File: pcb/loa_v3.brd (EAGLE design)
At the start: 50.9 x 81.4 mm, 111 parts, among them IC1 STM32F10XVXT6, IC2 M25P80MW, IC3 NAND_FLASH, IC4 MCP1825S-1202E/DB, IC5 NCP3170, IC6 AD7266SU, Q2 50.000, Q3 25.000, U1 6SLX9TQG144, X3 MINI-USB

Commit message: Cleanup
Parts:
- JP8: value (none) -> GND
- SJ2: value (none) -> WP
- SJ3: value (none) -> AGND-GND
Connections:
- net N$37 renamed VDDA
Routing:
- net P94: track 20.2 -> 22.2 mm
- net +3V3: track 630.6 -> 631.6 mm, vias 39 -> 40
- net GND: track 244.8 -> 245.7 mm, vias 55 -> 56
- net P93: track 17.7 -> 18.4 mm
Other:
- board text added: "GND"
- board text removed: "optional"
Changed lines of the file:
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@@
 <setting verticaltext="up"/>
 </settings>
-<grid distance="0.635" unitdist="mm" unit="mm" style="dots" multiple="1" display="yes" altdistance="0.00625" altunitdist="inch" altunit="inch"/>
+<grid distance="0.635" unitdist="mm" unit="mm" style="dots" multiple="1" display="yes" altdistance="0.003125" altunitdist="inch" altunit="inch"/>
 <layers>
 <layer number="1" name="Top" color="4" fill="1" visible="yes" active="yes"/>
@@
 <wire x1="38.5763" y1="2.3813" x2="37.9413" y2="3.0163" width="0.254" layer="49"/>
 <wire x1="37.9413" y1="3.0163" x2="37.3063" y2="2.3813" width="0.254" layer="49"/>
-<circle x="41.5926" y="6.9851" radius="0.3549" width="0.3048" layer="1"/>
+<circle x="42.2276" y="6.6676" radius="0.3549" width="0.3048" layer="1"/>
 <circle x="40.4813" y="80.4069" radius="0.2245" width="0.3048" layer="1"/>
 <circle x="41.5131" y="80.0894" radius="0.2245" width="0.3048" layer="1"/>
@@
 <text x="13.97" y="19.2882" size="0.8128" layer="1" ratio="20" rot="SR270">05/2014</text>
 <text x="42.97995" y="77.62325" size="1.016" layer="1" ratio="15">v3</text>
-<text x="29.05125" y="78.26375" size="1.016" layer="21" ratio="12">optional</text>
 <circle x="18.57385" y="73.81885" radius="0.3549" width="0.3048" layer="1"/>
+<text x="12.54125" y="78.4225" size="1.016" layer="1" font="vector" ratio="15" rot="SR90">GND</text>
 </plain>
 <attributes>
@@
 <element name="C1" library="rcl" package="C0603" value="100n" x="39.37" y="77.47" rot="MR0"/>
 <element name="C2" library="rcl" package="C0603" value="100n" x="39.37" y="53.975" rot="MR0"/>
-<element name="SJ2" library="rca_sontiges" package="SJ_2S" value="" x="38.25875" y="49.53" rot="MR0"/>
-<element name="SJ3" library="rca_sontiges" package="SJS" value="" x="12.065" y="69.5325" rot="MR180"/>
+<element name="SJ2" library="rca_sontiges" package="SJ_2S" value="WP" x="38.25875" y="49.53" rot="MR0"/>
+<element name="SJ3" library="rca_sontiges" package="SJS" value="AGND-GND" x="12.065" y="69.5325" rot="MR180"/>
 <element name="JP7" library="pinhead2" package="2X16" value="" x="48.26" y="20.32" rot="R270"/>
-<element name="JP8" library="pinhead2" package="1X01" value="" x="13.97" y="80.01"/>
+<element name="JP8" library="pinhead2" package="1X01" value="GND" x="13.97" y="80.01"/>
 </elements>
 <signals>
@@
 <wire x1="10.0013" y1="39.5288" x2="10.0013" y2="39.8462" width="0.8128" layer="16"/>
 <wire x1="10.0013" y1="39.8462" x2="10.00125" y2="40.3225" width="0.8128" layer="16"/>
-<wire x1="39.6" y1="23.5825" x2="37.845" y2="23.5825" width="0.3048" layer="1"/>
-<wire x1="40.005" y1="23.1775" x2="39.6" y2="23.5825" width="0.3048" layer="1"/>
-<wire x1="40.5374" y1="23.1775" x2="40.005" y2="23.1775" width="0.3048" layer="1"/>
+<wire x1="39.75875" y1="23.5825" x2="37.845" y2="23.5825" width="0.3048" layer="1"/>
+<wire x1="40.16375" y1="23.1775" x2="39.75875" y2="23.5825" width="0.3048" layer="1"/>
+<wire x1="40.5374" y1="23.1775" x2="40.16375" y2="23.1775" width="0.3048" layer="1"/>
 <wire x1="40.6399" y1="23.28" x2="40.5374" y2="23.1775" width="0.3048" layer="1"/>
 <wire x1="40.6399" y1="23.0189" x2="40.6399" y2="23.28" width="0.3048" layer="1"/>
@@
 <wire x1="13.81125" y1="69.5325" x2="13.97" y2="69.69125" width="0.3048" layer="16"/>
 <contactref element="JP8" pad="1"/>
+<via x="41.671875" y="23.33625" extent="1-16" drill="0.3048"/>
+<wire x1="41.671875" y1="23.33625" x2="40.69635" y2="23.33625" width="0.6096" layer="1"/>
 </signal>
 <signal name="+3V3">
@@
 <wire x1="30.4801" y1="29.185" x2="30.8437" y2="29.2813" width="0.8128" layer="16"/>
 <wire x1="27.4637" y1="30.06" x2="27.5038" y2="30.1001" width="0.8128" layer="16"/>
-<wire x1="37.845" y1="24.0825" x2="39.4812" y2="24.0825" width="0.3048" layer="1"/>
-<wire x1="39.4812" y1="24.0825" x2="40.3225" y2="24.9238" width="0.3048" layer="1"/>
-<wire x1="40.3225" y1="24.9238" x2="40.5837" y2="24.9238" width="0.3048" layer="1"/>
+<wire x1="37.845" y1="24.0825" x2="39.63995" y2="24.0825" width="0.3048" layer="1"/>
+<wire x1="39.63995" y1="24.0825" x2="40.48125" y2="24.9238" width="0.3048" layer="1"/>
+<wire x1="40.48125" y1="24.9238" x2="40.5837" y2="24.9238" width="0.3048" layer="1"/>
 <wire x1="40.5837" y1="24.9238" x2="40.6399" y2="24.98" width="0.3048" layer="1"/>
 <wire x1="37.845" y1="21.5825" x2="39.4651" y2="21.5825" width="0.3048" layer="1"/>
@@
 <wire x1="40.6399" y1="24.98" x2="40.6399" y2="24.92385" width="0.6096" layer="1"/>
 <wire x1="40.6399" y1="24.92385" x2="40.79875" y2="24.765" width="0.6096" layer="1"/>
-<wire x1="40.79875" y1="24.765" x2="41.75125" y2="24.765" width="0.6096" layer="1"/>
-<via x="41.75125" y="24.765" extent="1-16" drill="0.3048"/>
+<wire x1="40.79875" y1="24.765" x2="41.671875" y2="24.765" width="0.6096" layer="1"/>
+<via x="41.671875" y="24.765" extent="1-16" drill="0.3048"/>
 <via x="10.0012" y="21.2725" extent="1-16" drill="0.5"/>
 <wire x1="9.0487" y1="20.32" x2="9.04875" y2="20.32" width="0.8128" layer="1"/>
@@
 <vertex x="11.58875" y="26.19375"/>
 </polygon>
+<via x="39.449375" y="22.939375" extent="1-16" drill="0.3048"/>
+<wire x1="39.84625" y1="21.9075" x2="39.449375" y2="22.939375" width="0.6096" layer="1"/>
 </signal>
 <signal name="!RESET">
@@
 <via x="35.4012" y="19.2088" extent="1-16" drill="0.3048"/>
 </signal>
-<signal name="N$37">
+<signal name="VDDA">
 <contactref element="IC1" pad="22"/>
 <contactref element="C63" pad="1"/>
@@
 <wire x1="34.76625" y1="67.46875" x2="36.67125" y2="69.37375" width="0.254" layer="1"/>
 <contactref element="JP6" pad="12"/>
-<wire x1="36.67125" y1="69.37375" x2="43.02125" y2="69.37375" width="0.254" layer="1"/>
-<wire x1="43.02125" y1="69.37375" x2="46.355" y2="66.04" width="0.254" layer="1"/>
-<wire x1="46.355" y1="66.04" x2="48.26" y2="66.04" width="0.254" layer="1"/>
+<wire x1="36.67125" y1="69.37375" x2="39.21125" y2="69.37375" width="0.254" layer="1"/>
+<wire x1="39.21125" y1="69.37375" x2="42.545" y2="66.04" width="0.254" layer="1"/>
+<wire x1="42.545" y1="66.04" x2="48.26" y2="66.04" width="0.254" layer="1"/>
 <wire x1="48.26" y1="66.04" x2="49.53" y2="67.31" width="0.254" layer="1"/>
 </signal>
@@
 <wire x1="34.29" y1="67.78625" x2="36.35375" y2="69.85" width="0.254" layer="1"/>
 <contactref element="JP6" pad="11"/>
-<wire x1="36.35375" y1="69.85" x2="44.45" y2="69.85" width="0.254" layer="1"/>
-<wire x1="44.45" y1="69.85" x2="46.99" y2="67.31" width="0.254" layer="1"/>
+<wire x1="36.35375" y1="69.85" x2="39.37" y2="69.85" width="0.254" layer="1"/>
+<wire x1="39.37" y1="69.85" x2="42.70375" y2="66.51625" width="0.254" layer="1"/>
+<wire x1="42.70375" y1="66.51625" x2="46.19625" y2="66.51625" width="0.254" layer="1"/>
+<wire x1="46.19625" y1="66.51625" x2="46.99" y2="67.31" width="0.254" layer="1"/>
 </signal>
 <signal name="P94">
 <contactref element="U1" pad="P94"/>
 <contactref element="JP6" pad="10"/>
-<wire x1="36.228375" y1="70.3263" x2="43.815" y2="70.3263" width="0.254" layer="1"/>
-<wire x1="43.815" y1="70.3263" x2="45.72" y2="70.32625" width="0.254" layer="1"/>
-<wire x1="45.72" y1="70.32625" x2="46.275625" y2="70.881875" width="0.254" layer="1"/>
-<wire x1="46.275625" y1="70.881875" x2="48.498125" y2="70.881875" width="0.254" layer="1"/>
-<wire x1="48.498125" y1="70.881875" x2="49.53" y2="69.85" width="0.254" layer="1"/>
+<wire x1="36.228375" y1="70.3263" x2="39.5287" y2="70.3263" width="0.254" layer="1"/>
+<wire x1="48.180625" y1="68.500625" x2="49.53" y2="69.85" width="0.254" layer="1"/>
 <wire x1="32.127046875" y1="65.748721875" x2="33.81375" y2="67.435425" width="0.254" layer="1"/>
 <wire x1="33.81375" y1="67.435425" x2="33.81375" y2="67.945" width="0.254" layer="1"/>
 <wire x1="33.81375" y1="67.945" x2="36.228375" y2="70.3263" width="0.254" layer="1"/>
+<wire x1="48.180625" y1="68.500625" x2="46.593125" y2="68.500625" width="0.254" layer="1"/>
+<wire x1="46.593125" y1="68.500625" x2="45.085" y2="66.9925" width="0.254" layer="1"/>
+<wire x1="45.085" y1="66.9925" x2="42.8625" y2="66.9925" width="0.254" layer="1"/>
+<wire x1="42.8625" y1="66.9925" x2="39.5287" y2="70.3263" width="0.254" layer="1"/>
 </signal>
 <signal name="P95">

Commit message: Changed logo to reflect the version number
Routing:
- net +3V3: track 631.6 -> 635.4 mm
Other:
- board text added: "v3.0"
- board text removed: "v3"
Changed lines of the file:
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@@
 <?xml version="1.0" encoding="utf-8"?>
 <!DOCTYPE eagle SYSTEM "eagle.dtd">
-<eagle version="6.5.0">
+<eagle version="6.4">
 <drawing>
 <settings>
@@
 <setting verticaltext="up"/>
 </settings>
-<grid distance="0.635" unitdist="mm" unit="mm" style="dots" multiple="1" display="yes" altdistance="0.003125" altunitdist="inch" altunit="inch"/>
+<grid distance="0.635" unitdist="mm" unit="mm" style="dots" multiple="1" display="yes" altdistance="0.00625" altunitdist="inch" altunit="inch"/>
 <layers>
 <layer number="1" name="Top" color="4" fill="1" visible="yes" active="yes"/>
@@
 <wire x1="37.9413" y1="3.0163" x2="37.3063" y2="2.3813" width="0.254" layer="49"/>
 <circle x="42.2276" y="6.6676" radius="0.3549" width="0.3048" layer="1"/>
-<circle x="40.4813" y="80.4069" radius="0.2245" width="0.3048" layer="1"/>
-<circle x="41.5131" y="80.0894" radius="0.2245" width="0.3048" layer="1"/>
+<circle x="40.401925" y="80.0894" radius="0.2245" width="0.3048" layer="1"/>
+<circle x="41.1956" y="80.645025" radius="0.2245" width="0.3048" layer="1"/>
 <circle x="38.5762" y="79.4544" radius="0.3" width="0.254" layer="1"/>
 <text x="19.2088" y="0.635" size="1.27" layer="1" ratio="15">R</text>
 <text x="39.68745" y="34.29015" size="1.4224" layer="1" ratio="15" rot="R180">fg</text>
 <text x="13.97" y="19.2882" size="0.8128" layer="1" ratio="20" rot="SR270">05/2014</text>
-<text x="42.97995" y="77.62325" size="1.016" layer="1" ratio="15">v3</text>
+<text x="38.21745" y="74.607" size="1.016" layer="1" ratio="15">v3.0</text>
 <circle x="18.57385" y="73.81885" radius="0.3549" width="0.3048" layer="1"/>
 <text x="12.54125" y="78.4225" size="1.016" layer="1" font="vector" ratio="15" rot="SR90">GND</text>
+<circle x="41.8306" y="79.851275" radius="0.2245" width="0.3048" layer="1"/>
 </plain>
 <attributes>
@@
 <wire x1="45.9581" y1="75.9618" x2="45.72" y2="76.3588" width="0.3048" layer="1" curve="36.872784"/>
 <wire x1="45.72" y1="76.3588" x2="42.7038" y2="77.1525" width="0.3048" layer="1"/>
-<wire x1="42.7038" y1="77.1525" x2="41.4338" y2="77.9463" width="0.3048" layer="1"/>
-<wire x1="42.5451" y1="78.7401" x2="41.4338" y2="77.9463" width="0.3048" layer="1"/>
-<wire x1="42.5451" y1="79.0576" x2="42.5451" y2="78.7401" width="0.3048" layer="1"/>
-<wire x1="42.3863" y1="79.2163" x2="42.5451" y2="79.0576" width="0.3048" layer="1"/>
-<wire x1="42.0688" y1="79.2163" x2="42.3863" y2="79.2163" width="0.3048" layer="1"/>
-<wire x1="40.7988" y1="78.5813" x2="41.1163" y2="78.74" width="0.3048" layer="1"/>
-<wire x1="41.1163" y1="78.74" x2="42.0688" y2="79.2163" width="0.3048" layer="1"/>
-<wire x1="39.8463" y1="78.5813" x2="40.4813" y2="78.5813" width="0.3048" layer="1"/>
-<wire x1="40.4813" y1="78.5813" x2="40.7988" y2="78.5813" width="0.3048" layer="1"/>
+<wire x1="42.7038" y1="77.1525" x2="41.671925" y2="77.78755" width="0.3048" layer="1"/>
+<wire x1="42.70385" y1="78.58135" x2="41.671925" y2="77.78755" width="0.3048" layer="1"/>
+<wire x1="42.70385" y1="78.89885" x2="42.70385" y2="78.58135" width="0.3048" layer="1"/>
+<wire x1="42.465675" y1="79.05755" x2="42.70385" y2="78.89885" width="0.3048" layer="1"/>
+<wire x1="42.148175" y1="79.05755" x2="42.465675" y2="79.05755" width="0.3048" layer="1"/>
+<wire x1="40.7988" y1="78.5813" x2="40.91783125" y2="78.620953125" width="0.3048" layer="1"/>
+<wire x1="40.91783125" y1="78.620953125" x2="41.036925" y2="78.660625" width="0.3048" layer="1"/>
+<wire x1="41.036925" y1="78.660625" x2="41.65031875" y2="78.879721875" width="0.3048" layer="1"/>
+<wire x1="41.65031875" y1="78.879721875" x2="42.148175" y2="79.05755" width="0.3048" layer="1"/>
+<wire x1="39.8463" y1="78.5813" x2="40.7988" y2="78.5813" width="0.3048" layer="1"/>
 <wire x1="39.8463" y1="79.2163" x2="39.8463" y2="78.5813" width="0.3048" layer="1"/>
 <wire x1="39.5289" y1="80.1688" x2="39.8463" y2="79.2163" width="0.3048" layer="1" curve="-30.476126"/>
@@
 <wire x1="39.8463" y1="77.6288" x2="39.5288" y2="77.9463" width="0.3048" layer="1"/>
 <wire x1="38.5763" y1="76.6763" x2="39.8463" y2="77.6288" width="0.3048" layer="1"/>
-<wire x1="40.4813" y1="78.5813" x2="40.4813" y2="80.1688" width="0.254" layer="1"/>
-<wire x1="41.1163" y1="78.74" x2="41.4338" y2="79.8513" width="0.254" layer="1"/>
-<wire x1="41.1163" y1="78.74" x2="40.7988" y2="77.6288" width="0.254" layer="1"/>
-<wire x1="40.4813" y1="78.5813" x2="40.4813" y2="77.9463" width="0.254" layer="1"/>
 <wire x1="40.22" y1="77.47" x2="40.0612" y2="77.6288" width="0.3048" layer="16"/>
 <wire x1="40.0612" y1="77.6288" x2="39.8463" y2="77.6288" width="0.3048" layer="16"/>
@@
 <via x="39.449375" y="22.939375" extent="1-16" drill="0.3048"/>
 <wire x1="39.84625" y1="21.9075" x2="39.449375" y2="22.939375" width="0.6096" layer="1"/>
+<wire x1="41.195625" y1="77.866875" x2="41.75125" y2="79.6925" width="0.254" layer="1"/>
+<wire x1="41.11625" y1="80.406875" x2="40.878125" y2="78.184375" width="0.254" layer="1"/>
+<wire x1="40.401875" y1="79.85125" x2="40.48125" y2="77.94625" width="0.254" layer="1"/>
+<wire x1="40.878125" y1="78.184375" x2="40.91783125" y2="78.620953125" width="0.254" layer="1"/>
+<wire x1="41.195625" y1="77.866875" x2="41.513125" y2="78.819375" width="0.254" layer="1"/>
+<wire x1="41.513125" y1="78.819375" x2="41.65031875" y2="78.879721875" width="0.254" layer="1"/>
+<wire x1="40.48125" y1="77.94625" x2="40.48125" y2="78.58125" width="0.254" layer="1"/>
+<wire x1="40.48125" y1="78.58125" x2="40.16375" y2="78.58125" width="0.254" layer="1"/>
 </signal>
 <signal name="!RESET">
@@
 <wire x1="16.9864" y1="29.6863" x2="16.9864" y2="30.0038" width="0.254" layer="16"/>
 <wire x1="16.9864" y1="30.0038" x2="27.305" y2="40.3225" width="0.254" layer="16"/>
-<wire x1="27.305" y1="40.3225" x2="31.115" y2="40.3225" width="0.254" layer="16"/>
-<wire x1="31.115" y1="40.3225" x2="33.65505" y2="42.86255" width="0.254" layer="16"/>
+<wire x1="27.305" y1="40.3225" x2="27.46375" y2="40.48125" width="0.254" layer="16"/>
+<wire x1="27.46375" y1="40.48125" x2="31.27375" y2="40.48125" width="0.254" layer="16"/>
+<wire x1="31.27375" y1="40.48125" x2="33.65505" y2="42.86255" width="0.254" layer="16"/>
 <wire x1="18.09745" y1="29.6863" x2="16.9864" y2="29.6863" width="0.254" layer="1"/>
 <wire x1="18.70125" y1="29.0825" x2="18.09745" y2="29.6863" width="0.254" layer="1"/>
@@
 <wire x1="17.62125" y1="29.21" x2="17.6213" y2="29.3688" width="0.254" layer="16"/>
 <wire x1="17.6213" y1="29.3688" x2="17.6213" y2="30.0038" width="0.254" layer="16"/>
-<wire x1="17.6213" y1="30.0038" x2="25.55875" y2="37.94125" width="0.254" layer="16"/>
+<wire x1="17.6213" y1="30.0038" x2="25.4" y2="37.7825" width="0.254" layer="16"/>
 <via x="17.2245" y="28.8131" extent="1-16" drill="0.3048"/>
 <contactref element="RN4" pad="1"/>
-<wire x1="25.55875" y1="37.94125" x2="27.94" y2="37.94125" width="0.254" layer="16"/>
+<wire x1="25.4" y1="37.7825" x2="27.78125" y2="37.7825" width="0.254" layer="16"/>
 <wire x1="28.8237" y1="39.3583" x2="28.8237" y2="38.82495" width="0.254" layer="1"/>
 <wire x1="28.8237" y1="38.82495" x2="28.41625" y2="38.4175" width="0.254" layer="1"/>
 <via x="28.41625" y="38.4175" extent="1-16" drill="0.3048"/>
 <wire x1="28.41625" y1="38.4175" x2="28.09875" y2="38.1" width="0.254" layer="16"/>
-<wire x1="27.94" y1="37.94125" x2="28.41625" y2="38.4175" width="0.254" layer="16"/>
+<wire x1="27.78125" y1="37.7825" x2="28.41625" y2="38.4175" width="0.254" layer="16"/>
 </signal>
 <signal name="FSMC_D15">
@@
 <wire x1="26.51125" y1="40.16375" x2="26.5112" y2="41.2749" width="0.254" layer="1"/>
 <wire x1="26.5112" y1="41.2749" x2="26.5113" y2="41.275" width="0.254" layer="1"/>
-<wire x1="26.5113" y1="41.275" x2="30.7975" y2="41.275" width="0.254" layer="16"/>
-<wire x1="30.7975" y1="41.275" x2="33.33755" y2="43.81505" width="0.254" layer="16"/>
+<wire x1="26.5113" y1="41.275" x2="26.67" y2="41.43375" width="0.254" layer="16"/>
+<wire x1="26.67" y1="41.43375" x2="30.95625" y2="41.43375" width="0.254" layer="16"/>
+<wire x1="30.95625" y1="41.43375" x2="33.33755" y2="43.81505" width="0.254" layer="16"/>
 <via x="26.5113" y="41.275" extent="1-16" drill="0.3048"/>
 <contactref element="RN6" pad="2"/>
@@
 <wire x1="24.92375" y1="39.68755" x2="26.03505" y2="39.68755" width="0.254" layer="16"/>
 <wire x1="26.03505" y1="39.68755" x2="27.14625" y2="40.79875" width="0.254" layer="16"/>
-<wire x1="27.14625" y1="40.79875" x2="30.95625" y2="40.79875" width="0.254" layer="16"/>
-<wire x1="30.95625" y1="40.79875" x2="33.49625" y2="43.33875" width="0.254" layer="16"/>
+<wire x1="27.14625" y1="40.79875" x2="27.305" y2="40.9575" width="0.254" layer="16"/>
+<wire x1="27.305" y1="40.9575" x2="31.115" y2="40.9575" width="0.254" layer="16"/>
+<wire x1="31.115" y1="40.9575" x2="33.49625" y2="43.33875" width="0.254" layer="16"/>
 <wire x1="33.49625" y1="43.33875" x2="37.30625" y2="43.33875" width="0.254" layer="16"/>
 <via x="24.92375" y="39.68755" extent="1-16" drill="0.3048"/>

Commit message: Added BOM attributes
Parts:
- C57, C58: value 470n -> 1µ
- IC3: value NAND_FLASH -> S34ML04G100TFI000
- IC6: value AD7266SU -> AD7265SU
- L2, L4: value 0,68u -> 0,47u
- LED2: value Red -> Yellow

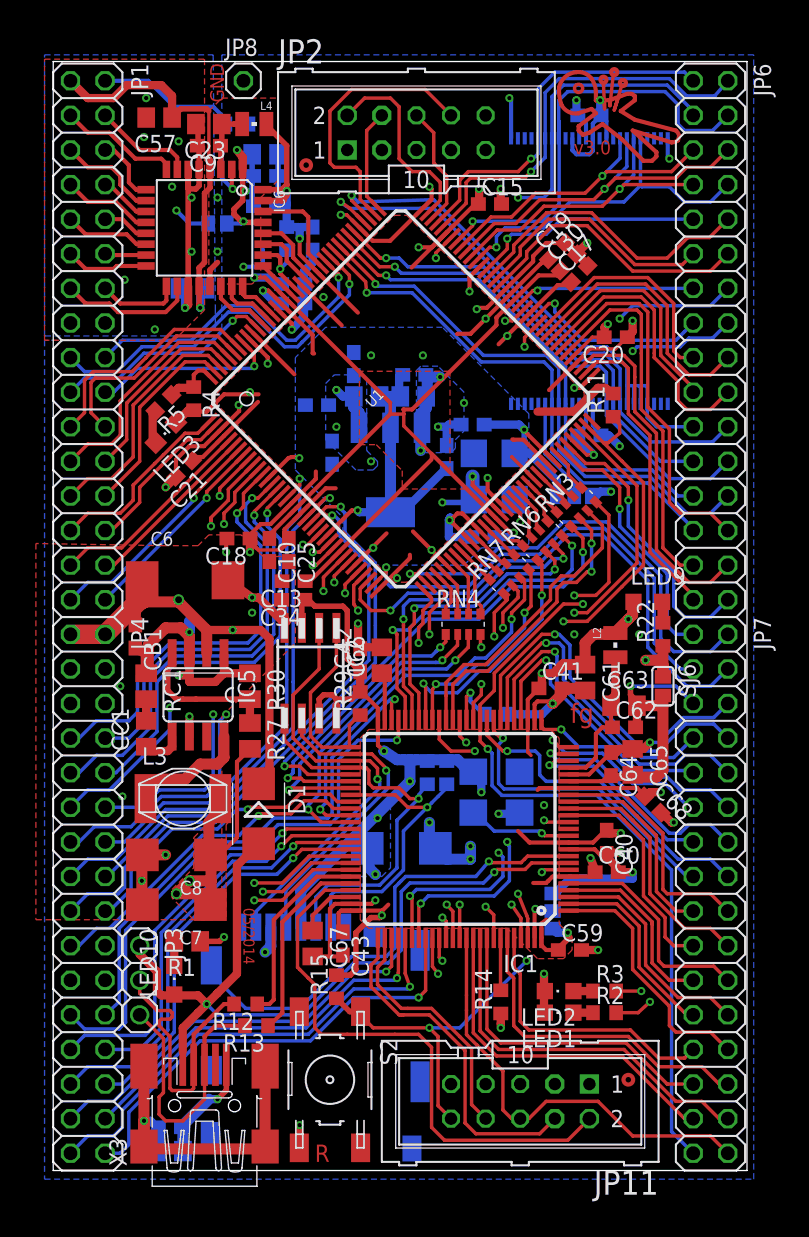
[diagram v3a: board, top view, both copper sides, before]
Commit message: Update NAND Flash Package, Reduces C type variations
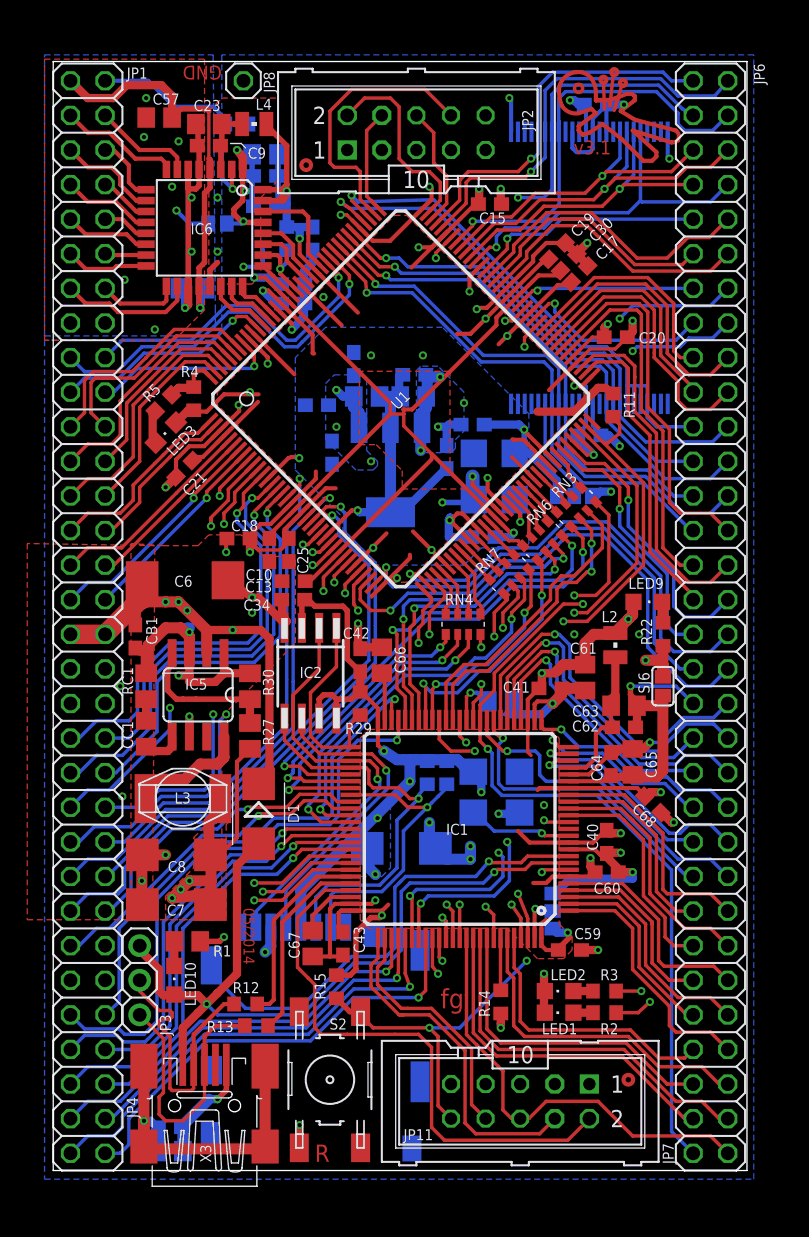
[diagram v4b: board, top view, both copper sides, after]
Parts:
- C61: value 4u7 -> 4µ7
- C62, C64: value 1n -> 10n
- C66, C67: value 2u2 -> 4µ7
- R1: value 820 -> 2k2
- R7: value 10k -> 2k2; device rcl:R0603 -> rcl:R0805
- moved R7 1.00 mm to (32.9, 34.4)
- moved C1 0.93 mm to (39.8, 78.3)
- moved IC3 0.16 mm to (39.4, 66.2)
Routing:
- net +3V3: track 635.4 -> 638.5 mm, vias 40 -> 41
- net GND: track 245.7 -> 248.7 mm
- net VCC: track 48.5 -> 50.2 mm, vias 3 -> 5
- net PB10: track 41.1 -> 42.7 mm
- net P101_IO3: track 34.1 -> 32.8 mm
- net PC6: track 31.4 -> 32.0 mm
- net P97_IO7: track 25.7 -> 26.4 mm
- net PROGRAM_B: track 15.2 -> 14.6 mm
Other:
- board text added: "v3.1"
- board text removed: "v3.0"
